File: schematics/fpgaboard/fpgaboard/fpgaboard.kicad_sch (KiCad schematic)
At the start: 1 part, among them U1 LFE5UM-85F-7BG381x

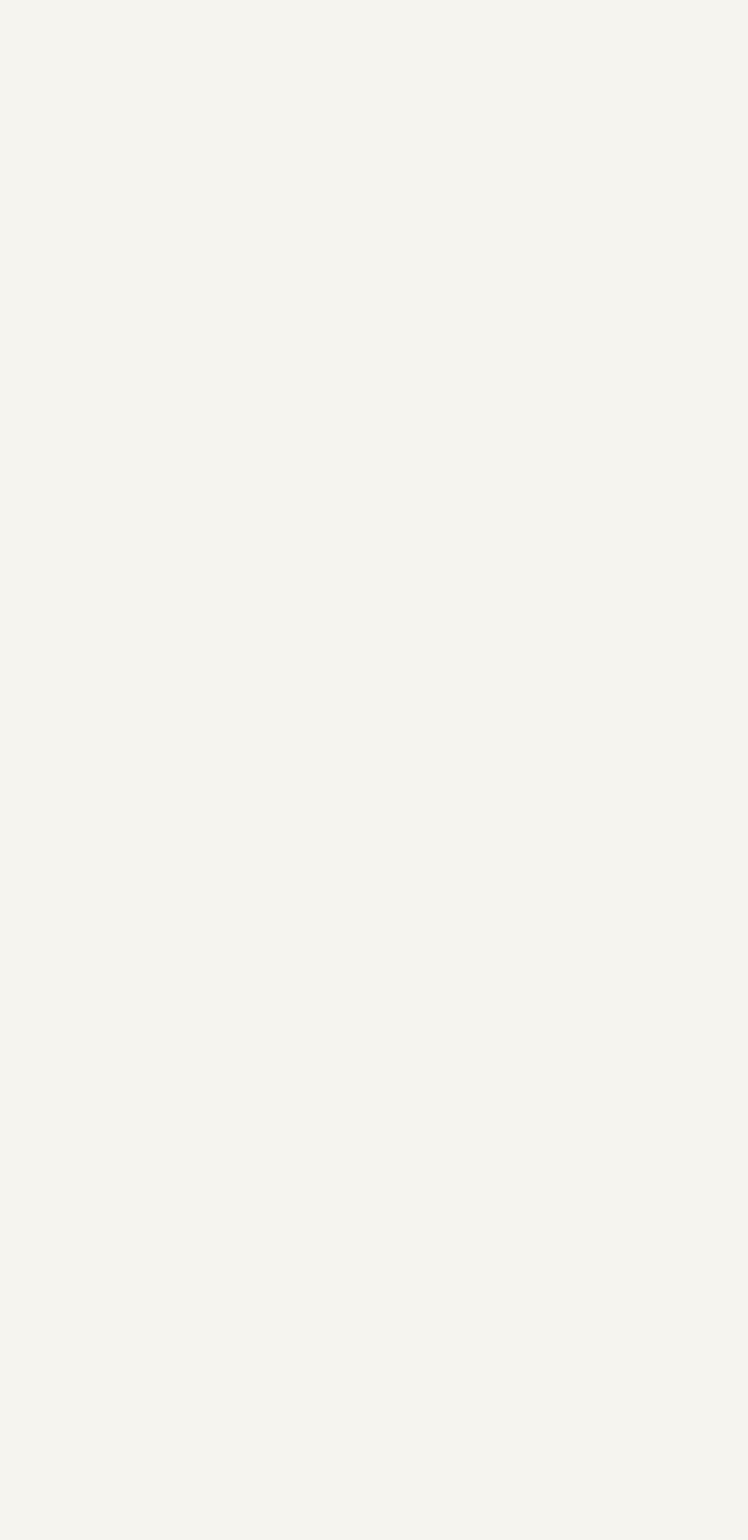
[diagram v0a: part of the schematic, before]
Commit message: Updated design rules for fpgaboard.
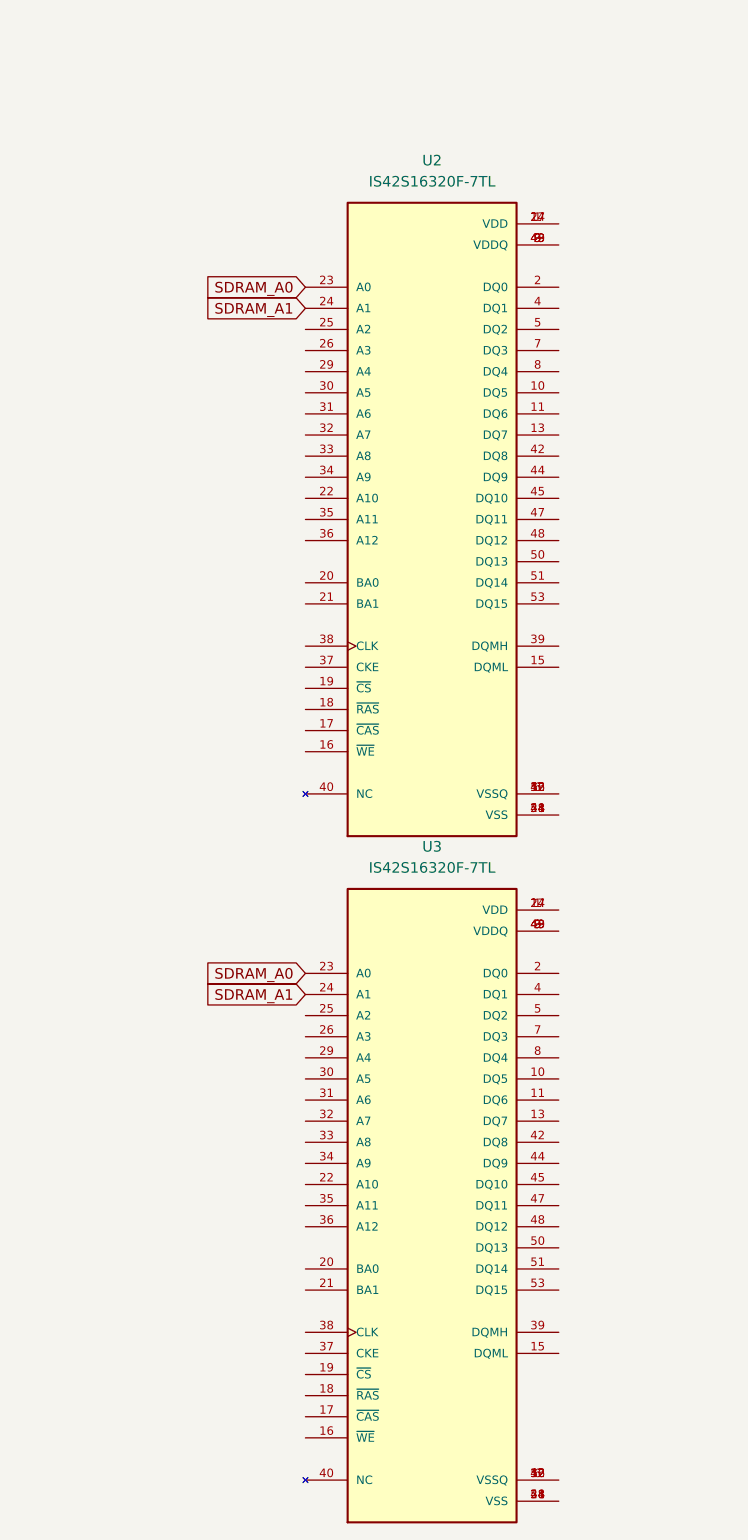
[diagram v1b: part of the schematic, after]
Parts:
- added U2, U3: IS42S16320F-7TL, IS42S16320F-7TL:SOP80P1176X120-54N, symbol IS42S16320F-7TL:IS42S16320F-7TL
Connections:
- new net: U2.1 (VDD), U2.14 (VDD), U2.27 (VDD)
- new net: U2.12 (VSSQ), U2.46 (VSSQ), U2.52 (VSSQ), U2.6 (VSSQ)
- new net: U2.28 (VSS), U2.41 (VSS), U2.54 (VSS)
- new net: U2.3 (VDDQ), U2.43 (VDDQ), U2.49 (VDDQ), U2.9 (VDDQ)
- new net: U3.1 (VDD), U3.14 (VDD), U3.27 (VDD)
- new net: U3.12 (VSSQ), U3.46 (VSSQ), U3.52 (VSSQ), U3.6 (VSSQ)
- new net: U3.28 (VSS), U3.41 (VSS), U3.54 (VSS)
- new net: U3.3 (VDDQ), U3.43 (VDDQ), U3.49 (VDDQ), U3.9 (VDDQ)
- new net SDRAM_A0: U2.23 (A0), U3.23 (A0)
- new net SDRAM_A1: U2.24 (A1), U3.24 (A1)

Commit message: Work on custom FPGA board with more RAM and beefier FPGA.
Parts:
- removed U1: LFE5UM-85F-7BG381x, Package_BGA:Lattice_caBGA-381_17x17mm_Layout20x20_P0.8mm, symbol FPGA_Lattice:LFE5UM-85F-7BG381x
- removed U2, U3: IS42S16320F-7TL, IS42S16320F-7TL:SOP80P1176X120-54N, symbol IS42S16320F-7TL:IS42S16320F-7TL
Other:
- added sheet FPGA (FPGA.kicad_sch)
- added sheet POWER (POWER.kicad_sch)
- added sheet RAM (RAM.kicad_sch)
